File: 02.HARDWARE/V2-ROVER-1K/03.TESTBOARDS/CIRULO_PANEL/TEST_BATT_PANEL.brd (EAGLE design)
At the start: 36 x 57.3 mm, 14 parts, among them J1 302-S201, Q1 PJA3416AE_R1_00001, U3 ATE1D-5M3-10-Z

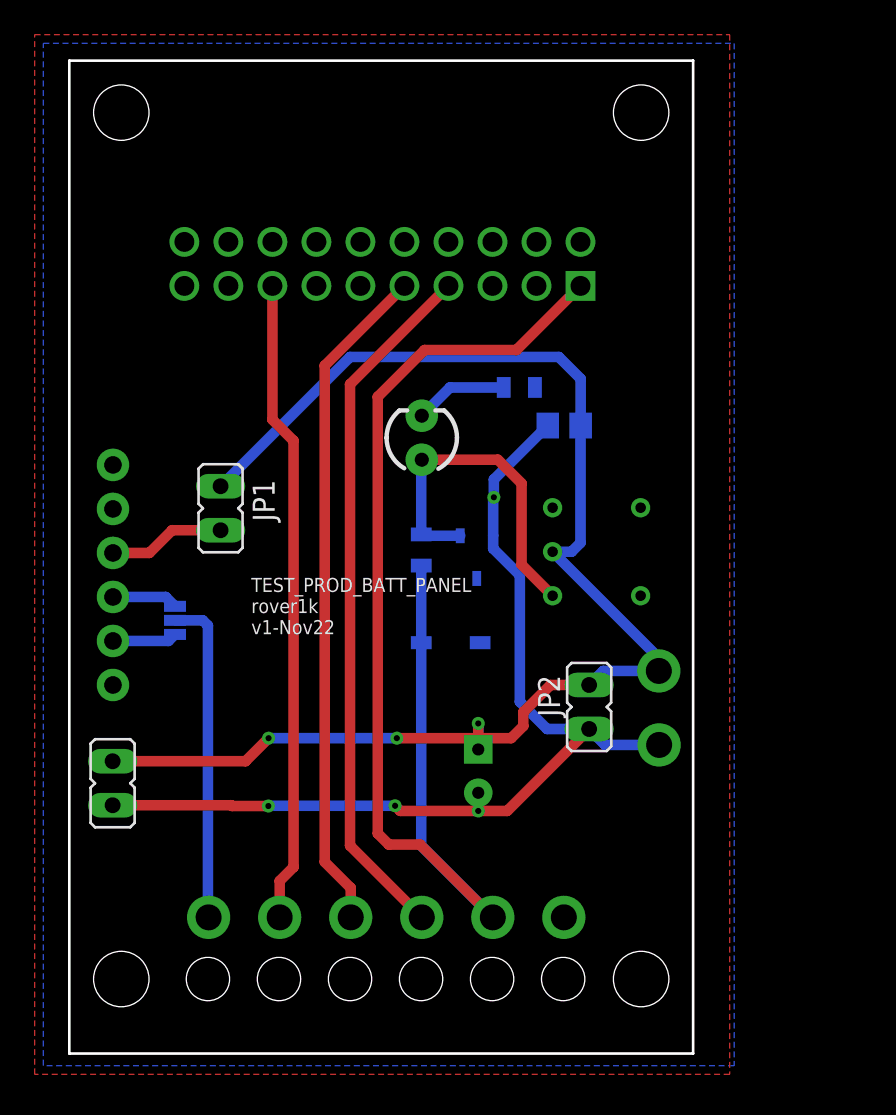
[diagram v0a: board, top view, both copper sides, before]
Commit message: Versiones v2 pendientes de revision de conjunto de PCBs Cirulo programacion.
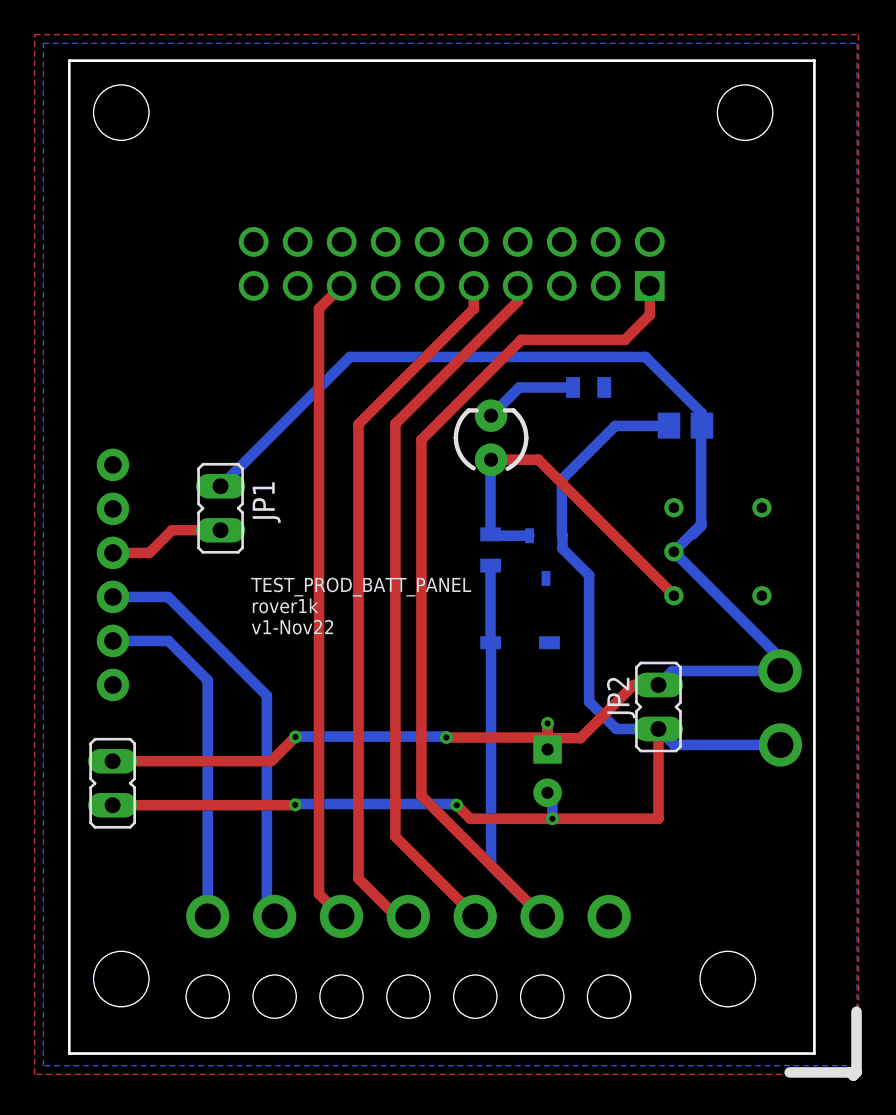
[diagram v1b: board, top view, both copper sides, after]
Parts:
- removed JP3: JUMPER-SMT_3_1-NC_PASTE_NO-SILK, SparkFun-Jumpers:SMT-JUMPER_3_1-NC_PASTE_NO-SILK
- moved C13 7.00 mm to (50.6, 75.9)
- moved U3 7.00 mm to (55.0, 71.2)
- moved C1 4.00 mm to (42.6, 56.0)
- moved D3 4.00 mm to (39.3, 75.2)
- moved FUSE 4.00 mm to (39.3, 68.8)
- moved J1 4.00 mm to (48.5, 84.0)
- moved JP2 4.00 mm to (49.0, 59.7)
- moved Q1 4.00 mm to (42.5, 68.3)
- moved R40 4.00 mm to (45.0, 78.1)
- moved Z1 4.00 mm to (41.0, 63.4)
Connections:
- removed net N$2: J2.2, JP3.1
- removed net N$3: J2.3, JP3.3
- new net RXI: J2.3
- net TXO: now also J2.2; no longer JP3.2
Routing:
- net RXI: track 0.00 -> 24.2 mm, vias 0 -> 1
- net GND_PSU: track 57.6 -> 71.7 mm, vias 5 -> 4
- net VCC_PSU: track 81.6 -> 94.2 mm
- net N$3: track 3.80 -> 0.00 mm
- net N$2: track 3.74 -> 0.00 mm
- net SWCLK: track 39.0 -> 40.7 mm
- net TXO: track 18.9 -> 20.0 mm
- net SWDIO: track 40.5 -> 41.2 mm
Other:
- board size 36 x 57.3 mm -> 43 x 57.3 mm
